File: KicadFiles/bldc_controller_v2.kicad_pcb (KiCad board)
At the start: 4 copper layers, 99.1 x 99.1 mm, 184 parts, among them J1 Conn_01x06_Male, J2 Screw_Terminal_01x04, Q1 2N7002E, Q10 IRLB8721PBF, Q11 IRLB8721PBF, Q2 DMN65D8L-7, Q3 DMN65D8L-7, Q4 MMBT3904, Q5 IRF4905, Q6 IRLB8721PBF, Q7 IRLB8721PBF, Q8 IRLB8721PBF, Q9 IRLB8721PBF, SW1 1301.9314, SW2 D6C50 F1 LFS, SW3 D6C40 F1 LFS, U1 ATmega328P-PU, U10 IRS2004, U2 SN74LVC1G11DBVR, U3 uA7810, U4 LM7805_TO220, U5 CD4044BE, U6 LM339, U7 MCP601-xP, U8 IRS2004, U9 IRS2004, Y1 9B-16.000MBBK-B

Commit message: Ready for Parts Placement
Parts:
- removed C37: 0.1uF, Capacitor_SMD:C_0805_2012Metric_Pad1.15x1.40mm_HandSolder
- removed R53: 0, Resistor_SMD:R_0805_2012Metric_Pad1.15x1.40mm_HandSolder
- removed REF** (x18): TestPoint_Plated_Hole_D2.0mm, TestPoint:TestPoint_Plated_Hole_D2.0mm
- removed RV1: 5K, Potentiometer_SMD:Trimmer_Pot_SM
- removed U10, U9: IRS2004, Package_DIP:DIP-8_W7.62mm
- added D7: LTST-C171GKT, LED_SMD:LED_0805_2012Metric_Pad1.15x1.40mm_HandSolder, F.Cu at (74.6, 36.0)
- added FB2: BL01RN1A1D2B, Ferrite_THT:Ferrite_Bead_TH, F.Cu at (50.0, 28.5)
- added J10: Conn_01x02_Female, Connector_PinHeader_2.54mm:PinHeader_1x02_P2.54mm_Vertical, F.Cu at (109.6, 18.1)
- added J11: Conn_01x02_Female, Connector_PinHeader_2.54mm:PinHeader_1x02_P2.54mm_Vertical, F.Cu at (100.4, 24.1)
- added J12: Conn_01x02_Female, Connector_PinHeader_2.54mm:PinHeader_1x02_P2.54mm_Vertical, F.Cu at (57.6, 67.4)
- added J13: Conn_01x02_Female, Connector_PinHeader_2.54mm:PinHeader_1x02_P2.54mm_Vertical, F.Cu at (94.4, 31.3)
- added J14: Conn_01x02_Female, Connector_PinHeader_2.54mm:PinHeader_1x02_P2.54mm_Vertical, F.Cu at (53.0, 67.4)
- added J15: Conn_01x04_Male, Connector_PinHeader_2.54mm:PinHeader_1x04_P2.54mm_Vertical, F.Cu at (41.4, 50.6)
- added J3: Conn_01x03_Male, Connector_PinHeader_2.54mm:PinHeader_1x03_P2.54mm_Vertical, F.Cu at (53.0, 57.7)
- added J4: Screw_Terminal, Connector:Terminal_Block_4Pin_TH, F.Cu at (60.5, 20.9)
- added J5: Conn_01x02_Female, Connector_PinHeader_2.54mm:PinHeader_1x02_P2.54mm_Vertical, F.Cu at (62.3, 57.7)
- added J9: Conn_01x02_Female, Connector_PinHeader_2.54mm:PinHeader_1x02_P2.54mm_Vertical, F.Cu at (95.8, 24.1)
- added JP2: SolderJumper_2_Open, Jumper:Solder_Jumper_2_Pin_5A, F.Cu at (118.0, 35.3)
- added SW4: 1301.9314, Button_Switch_SMD:Tactile_Switch_SM, F.Cu at (34.0, 47.0)
- added SW5: SW_Push_DPDT, Button_Switch_SMD:Slide_Switch_DPDT_SMD, F.Cu at (87.0, 33.2)
- added TP31: TestPoint, TestPoint:TestPoint_THTPad_1.0x1.0mm_Drill0.5mm, F.Cu at (105.3, 52.9)
- added TP32: TestPoint, TestPoint:TestPoint_THTPad_1.0x1.0mm_Drill0.5mm, F.Cu at (110.0, 49.8)
- added TP33: TestPoint, TestPoint:TestPoint_THTPad_1.0x1.0mm_Drill0.5mm, F.Cu at (114.5, 45.4)
- added TP34: TestPoint, TestPoint:TestPoint_THTPad_1.0x1.0mm_Drill0.5mm, F.Cu at (117.8, 42.3)
- added TP35: TestPoint, TestPoint:TestPoint_THTPad_1.0x1.0mm_Drill0.5mm, F.Cu at (85.1, 72.5)
- added TP36: TestPoint, TestPoint:TestPoint_THTPad_1.0x1.0mm_Drill0.5mm, F.Cu at (108.3, 52.9)
- added TP37: TestPoint, TestPoint:TestPoint_THTPad_1.0x1.0mm_Drill0.5mm, F.Cu at (118.6, 38.6)
- added TP38: TestPoint, TestPoint:TestPoint_THTPad_1.0x1.0mm_Drill0.5mm, F.Cu at (94.4, 67.1)
- C1, C2: value 10uF -> 47uF; footprint Capacitor_SMD:C_0805_2012Metric_Pad1.15x1.40mm_HandSolder -> Capacitor_THT:CP_Radial_D5.0mm_P2.00mm; moved to F.Cu
- C11: value 47uF -> 1uF; footprint Capacitor_THT:CP_Radial_D10.0mm_P5.00mm -> Capacitor_SMD:C_0805_2012Metric_Pad1.15x1.40mm_HandSolder
- C12, C23, C25, D11, D14, D15, D16, FB1, R21, R31, R33, R35, R37, R39, R40, R42: moved to F.Cu
- C13, C14, C22, C24, C3, C33: value 0.1uF -> 1uF; moved to F.Cu
- C15: value 22uF -> 22pF
- C16: value 1uF -> 22pF; moved to F.Cu
- C17, C21: value 1uF -> 0.1uF
- C18: value 22pF -> 0.1uF; moved to F.Cu
- C19: value 22pF -> 47uF; footprint Capacitor_SMD:C_0805_2012Metric_Pad1.15x1.40mm_HandSolder -> Capacitor_THT:CP_Radial_D5.0mm_P2.00mm; moved to F.Cu
- C20: value 0.1uF -> 1uF
- C26: value 0.1uF -> 15nF
- C27: value 10nF -> 0.1uF; moved to F.Cu
- C28, C29: value 22nF -> 0.1uF
- C30: value 22nF -> 1uF
- C31: value 1nF -> 1uF; moved to F.Cu
- C32: value 100pF -> 1uF; moved to F.Cu
- C34, C35: value 0.47uF -> 1uF
- C36: value 0.47uF -> 0.1uF
- C4: value 47uF -> 0.1uF; footprint Capacitor_THT:CP_Radial_D10.0mm_P5.00mm -> Capacitor_SMD:C_0805_2012Metric_Pad1.15x1.40mm_HandSolder
- C5: value 0.33uF -> 0.1uF; moved to F.Cu
- C6: value 0.22uF -> 0.1uF; moved to F.Cu
- C7: value 0.1uF -> 47uF; footprint Capacitor_SMD:C_0805_2012Metric_Pad1.15x1.40mm_HandSolder -> Capacitor_THT:CP_Radial_D5.0mm_P2.00mm
- C9: value 22uF -> 1uF
- D10: value BAT54HT1G -> LTST-C171TBKT; footprint Diode_SMD:D_SOD-323_HandSoldering -> LED_SMD:LED_0805_2012Metric_Pad1.15x1.40mm_HandSolder; moved to F.Cu
- D12: value SMF12A -> BAT54HT1G; footprint Diode_SMD:D_SOD-123F -> Diode_SMD:D_SOD-323_HandSoldering
- D13: value SMF5.0A -> BAT54HT1G; footprint Diode_SMD:D_SOD-123F -> Diode_SMD:D_SOD-323_HandSoldering
- D2: value LTST-C171KRKT -> SMF12A; footprint LED_SMD:LED_0805_2012Metric_Pad1.15x1.40mm_HandSolder -> Diode_SMD:D_SOD-123F
- D3, D6: value LTST-C171GKT -> LTST-C171KRKT
- D5: value LTST-C171KRKT -> SMF10A; footprint LED_SMD:LED_0805_2012Metric_Pad1.15x1.40mm_HandSolder -> Diode_SMD:D_SOD-123F
- D8: value SMF10A -> SMF5.0A
- D9: value LTST-C171TBKT -> LTST-C171GKT
- J2: value Screw_Terminal_01x04 -> Conn_01x03_Male; footprint Connector:Terminal_Block_4Pin_TH -> Connector_PinHeader_2.54mm:PinHeader_1x03_P2.54mm_Vertical
- Q1: value 2N7002E -> DMN65D8L-7
- Q4: value MMBT3904 -> DMN65D8L-7; moved to F.Cu
- R10, R13: value 300 -> 10K
- R11, R12: value 10K -> 100K; moved to F.Cu
- R14: value 10 -> 1K; moved to F.Cu
- R15: value 100K -> 50K; moved to F.Cu
- R16: value 1K -> 10K; moved to F.Cu
- R17: value 10K -> 1K; moved to F.Cu
- R19: value 3K -> 100K; moved to F.Cu
- R20: value 1K -> 100K
- R22: value 40K -> 100K
- R23: value 10K -> 0.47; footprint Resistor_SMD:R_0805_2012Metric_Pad1.15x1.40mm_HandSolder -> Resistor_THT:Power_Resistor_TH
- R24: value 1 -> 1K; footprint Resistor_THT:Power_Resistor_TH -> Resistor_SMD:R_0805_2012Metric_Pad1.15x1.40mm_HandSolder; moved to F.Cu
- R25: value 1 -> 0.47; moved to F.Cu
- R26, R27, R28: value 4.7 -> 10K; moved to F.Cu
- R29, R30: value 1 -> 10K; footprint Resistor_THT:Power_Resistor_TH -> Resistor_SMD:R_0805_2012Metric_Pad1.15x1.40mm_HandSolder; moved to F.Cu
- R32, R34, R36, R38: value 100K -> 10; moved to F.Cu
- R4: value 10K -> 300; moved to F.Cu
- R41: value 10 -> 100K; moved to F.Cu
- R43, R44, R45: value 10K -> 100K
- R46, R47, R48: value 1K -> 100K; moved to F.Cu
- R49, R50, R51, R9: value 1K -> 10K
- R52: value 0 -> 100; moved to F.Cu
- R6, R7: value 220 -> 300; moved to F.Cu
- R8: value 300 -> 10
- SW1: value 1301.9314 -> D6C50 F1 LFS; footprint Button_Switch_SMD:Tactile_Switch_SM -> Button_Switch_THT:Pushbutton_Switch_TH
- SW2: value D6C50 F1 LFS -> D6C40 F1 LFS
- SW3: value D6C40 F1 LFS -> 1301.9314; footprint Button_Switch_THT:Pushbutton_Switch_TH -> Button_Switch_SMD:Tactile_Switch_SM
- TP12, TP17, TP18, TP29: footprint TestPoint:TestPoint_Keystone_5000-5004_Miniature -> TestPoint:TestPoint_THTPad_1.0x1.0mm_Drill0.5mm
- U2: value SN74LVC1G11DBVR -> uA7810; footprint Package_TO_SOT_SMD:SOT-23-6_Handsoldering -> Package_TO_SOT_THT:TO-220-3_Vertical; moved to F.Cu
- U3: value uA7810 -> LM7805_TO220
- U4: value LM7805_TO220 -> MCP601-xP; footprint Package_TO_SOT_THT:TO-220-3_Vertical -> Package_DIP:DIP-8_W7.62mm
- U5: value CD4044BE -> LM339; footprint Package_DIP:DIP-16_W7.62mm -> Package_DIP:DIP-14_W7.62mm
- U6: value LM339 -> IRS2004; footprint Package_DIP:DIP-14_W7.62mm -> Package_DIP:DIP-8_W7.62mm
- U7: value MCP601-xP -> IRS2004
- moved U6 158.1 mm to (57.9, 28.0), turned to 0 degrees
- moved D16 142.8 mm to (43.4, 46.1), turned to 0 degrees
- moved D14 141.2 mm to (30.3, 49.9), turned to 0 degrees
- moved D15 141.1 mm to (36.1, 49.9), turned to 0 degrees
- moved C34 140.5 mm to (114.3, 17.3), turned to 0 degrees
- moved Q10 139.5 mm to (42.2, 70.4), turned to 0 degrees
- moved Q6 133.7 mm to (47.0, 53.4), turned to 0 degrees
- moved C35 131.9 mm to (99.1, 30.4), turned to 0 degrees
- moved R23 130.5 mm to (27.8, 56.0), turned to 0 degrees
- moved R49 129.9 mm to (76.7, 74.5), turned to 0 degrees
- moved U1 127.6 mm to (18.2, 17.9)
- moved C33 127.3 mm to (109.9, 24.5), turned to 0 degrees
- moved R25 124.4 mm to (27.8, 62.1), turned to 0 degrees
- moved TP16 123.4 mm to (122.0, 33.7)
- moved R21 123.1 mm to (38.7, 18.9), turned to 0 degrees
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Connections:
- C1 pad 1: /nRESET -> +BATT
- C1 pad 2: GNDD -> GNDPWR
- C10 pad 1: Vdrive -> +12V
- C10 pad 2: GNDPWR -> GNDD
- C11 pad 1: +12V -> +10V
- C11 pad 2: GNDPWR -> GNDD
- C12 pad 1: +5V -> +12V
- C12 pad 2: GNDD -> GNDPWR
- C13 pad 1: +10V -> /nSTART
- C14 pad 1: +5V -> /nESTOP
- C15 pad 1: +12V -> GNDD
- C15 pad 2: GNDPWR -> Net-(C15-Pad2)
- C17 pad 1: +12V -> +10V
- C17 pad 2: GNDPWR -> GNDD
- C18 pad 1: GNDD -> +5V
- C18 pad 2: Net-(C18-Pad2) -> GNDD
- C19 pad 1: Net-(C19-Pad1) -> /V_MOTOR
- C19 pad 2: GNDD -> GNDPWR
- C2 pad 1: /nESTOP -> VBUS
- C2 pad 2: GNDD -> GNDPWR
- C20 pad 1: +12V -> /V_MOTOR
- C21 pad 1: Vdrive -> /V_MOTOR
- C21 pad 2: Net-(C21-Pad2) -> GNDPWR
- C22 pad 1: +5V -> /AUX_IN
- C23 pad 1: GNDD -> +5V
- C23 pad 2: +10V -> GNDD
- C24 pad 1: GNDD -> /BTN_nRST
- C24 pad 2: +10V -> GNDD
- C25 pad 1: GNDD -> /V_MOTOR
- C25 pad 2: +10V -> /EFUSE_GATE
- C26 pad 1: +5V -> /I_FILT
- C27 pad 1: /I_RAW -> GNDD
- C27 pad 2: GNDD -> +10V
- C28 pad 1: Net-(C28-Pad1) -> GNDD
- C28 pad 2: PhaseA -> +10V
- C29 pad 1: Net-(C29-Pad1) -> GNDD
- C29 pad 2: PhaseB -> +10V
- C3 pad 1: Net-(C3-Pad1) -> VBUS
- C3 pad 2: GNDD -> GNDPWR
- C30 pad 2: PhaseC -> /PHASE_A
- C31 pad 1: /I_RAW -> Net-(C31-Pad1)
- C31 pad 2: GNDD -> /PHASE_B
- C32 pad 1: /I_RAW -> Net-(C32-Pad1)
- C32 pad 2: GNDD -> /PHASE_C
- C33 pad 1: +5V -> VBUS
- C33 pad 2: GNDD -> GNDPWR
- C34 pad 1: PhaseA -> VBUS
- C34 pad 2: GNDD -> GNDPWR
- C35 pad 1: PhaseB -> VBUS
- C35 pad 2: GNDD -> GNDPWR
- C36 pad 1: PhaseC -> +5V
- C4 pad 1: +BATT -> Net-(C4-Pad1)
- C4 pad 2: GNDPWR -> GNDD
- C5 pad 1: +12V -> VBUS
- C5 pad 2: GNDD -> GNDPWR
- C6 pad 1: +10V -> GNDD
- C6 pad 2: GNDD -> +5V
- C7 pad 1: GNDD -> +12V
- C7 pad 2: +5V -> GNDPWR
- C9 pad 1: Vdrive -> +12V
- D1 pad 2: +12V -> VBUS
- D10 pad 1: +5V -> Net-(D10-Pad1)
- D10 pad 2: /nRESET -> +5V
- D11 pad 2: /nESTOP -> /nSTART
- D12 pad 1: +12V -> +5V
- D12 pad 2: GNDD -> /nESTOP
- D13 pad 2: GNDD -> /BTN_nRST
- D14 pad 1: Net-(C28-Pad1) -> Net-(C30-Pad1)
- D15 pad 1: Net-(C29-Pad1) -> Net-(C31-Pad1)
- D16 pad 1: Net-(C30-Pad1) -> Net-(C32-Pad1)
- D2 pad 1: GNDD -> +12V
- D2 pad 2: Net-(D2-Pad2) -> GNDD
- D3 pad 2: VBUS -> +5V
- D4 pad 2: +10V -> +12V
- D5 pad 1: Net-(D5-Pad1) -> +10V
- D5 pad 2: +5V -> GNDD
- D8 pad 1: +10V -> +5V
- J1 pad 1: /nRESET -> /EXT_nRST
- J1 pad 2: /RXD -> +5V
- J1 pad 3: /TXD -> GNDD
- J1 pad 4: /ANALOG_IN -> GNDD
- J1 pad 5: +5V -> /TXD
- J1 pad 6: GNDD -> /RXD
- J2 pad 1: +BATT -> +5V
- J2 pad 2: Vdrive -> /I_THRESH
- J2 pad 3: GNDPWR -> GNDD
- JP1 pad 2: Vdrive -> /V_MOTOR
- Q1 pad 1: /nI_ERR -> /I_ERR
- Q1 pad 2: +5V -> GNDD
- Q10 pad 1: Net-(Q10-Pad1) -> /GATE_C_HI
- Q10 pad 3: PhaseC -> /PHASE_C
- Q11 pad 1: Net-(Q11-Pad1) -> /GATE_C_LO
- Q11 pad 2: PhaseC -> /PHASE_C
- Q5 pad 1: Net-(C21-Pad2) -> /EFUSE_GATE
- Q5 pad 3: Vdrive -> /V_MOTOR
- Q6 pad 1: Net-(Q6-Pad1) -> /GATE_A_HI
- Q6 pad 3: PhaseA -> /PHASE_A
- Q7 pad 1: Net-(Q7-Pad1) -> /GATE_A_LO
- Q7 pad 2: PhaseA -> /PHASE_A
- Q8 pad 1: Net-(Q8-Pad1) -> /GATE_B_HI
- Q8 pad 3: PhaseB -> /PHASE_B
- Q9 pad 1: Net-(Q9-Pad1) -> /GATE_B_LO
- Q9 pad 2: PhaseB -> /PHASE_B
- R10 pad 1: Net-(D6-Pad1) -> Net-(R10-Pad1)
- R11 pad 2: /nRESET -> /nSTART
- R13 pad 1: Net-(D9-Pad1) -> Net-(R13-Pad1)
- R13 pad 2: Net-(Q3-Pad3) -> GNDD
- R14 pad 1: Net-(R14-Pad1) -> Net-(Q4-Pad1)
- R14 pad 2: +10V -> /EFUSE_EN
- R15 pad 1: +5V -> /I_SENSE
- R15 pad 2: Net-(C16-Pad1) -> Net-(R15-Pad2)
- R16 pad 1: +5V -> Net-(R15-Pad2)
- R16 pad 2: /nI_ERR -> GNDD
- R17 pad 1: /EFUSE_EN -> +5V
- R17 pad 2: GNDD -> /nI_TRIG
- R18 pad 1: Vdrive -> Net-(Q4-Pad1)
- R18 pad 2: Net-(C21-Pad2) -> GNDD
- R19 pad 1: Net-(Q4-Pad1) -> /V_MOTOR
- R19 pad 2: /EFUSE_EN -> /EFUSE_GATE
- R2 pad 1: Net-(Q1-Pad3) -> Net-(D3-Pad1)
- R2 pad 2: Net-(D2-Pad2) -> Net-(Q1-Pad3)
- R20 pad 1: Net-(C21-Pad2) -> /AUX_IN
- R20 pad 2: Net-(Q4-Pad3) -> GNDD
- R22 pad 1: /I_SENSE -> +5V
- R22 pad 2: Net-(R22-Pad2) -> /BTN_nRST
- R23 pad 1: Net-(R22-Pad2) -> /I_RAW
- R23 pad 2: GNDD -> GNDPWR
- R24 pad 1: /I_RAW -> /EFUSE_GATE
- R24 pad 2: GNDPWR -> Net-(Q4-Pad3)
- R26 pad 1: Net-(D14-Pad2) -> +5V
- R26 pad 2: +10V -> Net-(R26-Pad2)
- R27 pad 1: Net-(D15-Pad2) -> /I_RAW
- R27 pad 2: +10V -> /I_FILT
- R28 pad 1: Net-(D16-Pad2) -> +5V
- R28 pad 2: +10V -> /BEMF_A
- R29 pad 1: /I_RAW -> +5V
- R29 pad 2: GNDPWR -> /BEMF_B
- R3 pad 1: Net-(D3-Pad1) -> Net-(D4-Pad1)
- R30 pad 1: /I_RAW -> +5V
- R30 pad 2: GNDPWR -> /BEMF_C
- R31 pad 1: Net-(Q6-Pad1) -> Net-(D14-Pad2)
- R31 pad 2: Net-(R31-Pad2) -> +10V
- R32 pad 1: Net-(Q6-Pad1) -> Net-(D15-Pad2)
- R32 pad 2: GNDD -> +10V
- R33 pad 1: Net-(Q7-Pad1) -> Net-(D16-Pad2)
- R33 pad 2: Net-(R33-Pad2) -> +10V
- R34 pad 1: Net-(Q7-Pad1) -> /GATE_A_LO
- R34 pad 2: GNDD -> Net-(R34-Pad2)
- R35 pad 1: Net-(Q8-Pad1) -> /GATE_B_LO
- R36 pad 1: Net-(Q8-Pad1) -> /GATE_C_LO
- R36 pad 2: GNDD -> Net-(R36-Pad2)
- R37 pad 1: Net-(Q9-Pad1) -> /GATE_A_HI
- R38 pad 1: Net-(Q9-Pad1) -> /GATE_B_HI
- R38 pad 2: GNDD -> Net-(R38-Pad2)
- R39 pad 1: Net-(Q10-Pad1) -> /GATE_C_HI
- R4 pad 1: /AUX_IN -> Net-(D6-Pad1)
- R4 pad 2: GNDD -> Net-(Q2-Pad3)
- R40 pad 1: Net-(Q10-Pad1) -> /GATE_A_HI
- R41 pad 1: Net-(Q11-Pad1) -> /GATE_A_LO
- R41 pad 2: Net-(R41-Pad2) -> GNDD
- R42 pad 1: Net-(Q11-Pad1) -> /GATE_B_HI
- R43 pad 1: /NEUTRAL -> /GATE_B_LO
- R43 pad 2: PhaseA -> GNDD
- R44 pad 1: /NEUTRAL -> /GATE_C_HI
- R44 pad 2: PhaseB -> GNDD
- R45 pad 1: /NEUTRAL -> /GATE_C_LO
- R45 pad 2: PhaseC -> GNDD
- R46 pad 1: +5V -> /PHASE_A
- R46 pad 2: /BEMF_A -> /A_FILT
- R47 pad 1: +5V -> /PHASE_B
- R47 pad 2: /BEMF_B -> /B_FILT
- R48 pad 1: +5V -> /PHASE_C
- R48 pad 2: /BEMF_C -> /C_FILT
- R49 pad 1: PhaseA -> /NEUTRAL
- R49 pad 2: Net-(R49-Pad2) -> /PHASE_A
- R5 pad 1: Net-(D4-Pad1) -> Net-(D7-Pad1)
- R50 pad 1: PhaseB -> /NEUTRAL
- R50 pad 2: Net-(R50-Pad2) -> /PHASE_B
- R51 pad 1: PhaseC -> /NEUTRAL
- R51 pad 2: Net-(R51-Pad2) -> /PHASE_C
- R52 pad 1: GNDPWR -> Net-(R52-Pad1)
- R52 pad 2: GNDD -> /nI_TRIG
- R6 pad 1: Net-(R6-Pad1) -> Net-(D9-Pad1)
- R7 pad 1: Net-(R7-Pad1) -> Net-(D10-Pad1)
- R7 pad 2: GNDD -> Net-(Q3-Pad3)
- R8 pad 1: Net-(D5-Pad1) -> Net-(R8-Pad1)
- R8 pad 2: Net-(Q2-Pad3) -> +10V
- R9 pad 1: +5V -> Net-(R9-Pad1)
- R9 pad 2: Net-(R9-Pad2) -> GNDD
- SW1 pad 1: /AUX_IN -> /nSTART
- SW1 pad 2: Net-(R9-Pad2) -> Net-(R9-Pad1)
- SW2 pad 1: /nRESET -> Net-(R10-Pad1)
- SW2 pad 2: Net-(R6-Pad1) -> /nESTOP
- SW3 pad 1: Net-(R7-Pad1) -> /BTN_nRST
- SW3 pad 2: /nESTOP -> Net-(R13-Pad1)
- TP1 pad 1: /I_RAW -> +12V
- TP10 pad 1: Net-(Q8-Pad1) -> /PHASE_A
- TP11 pad 1: Net-(Q10-Pad1) -> /EFUSE_GATE
- TP12 pad 1: GNDD -> /MCU_A_SIG
- TP13 pad 1: /BEMF_A -> /BEMF_B
- TP14 pad 1: /BEMF_B -> /I_FILT
- TP15 pad 1: /BEMF_C -> /GATE_A_LO
- TP16 pad 1: /NEUTRAL -> /PHASE_B
- TP17 pad 1: GNDD -> +5V
- TP18 pad 1: GNDPWR -> GNDD
- TP19 pad 1: /MCU_A_EN -> /EFUSE_EN
- TP2 pad 1: /nI_ERR -> GNDD
- TP20 pad 1: /MCU_C_SIG -> /MCU_B_EN
- TP21 pad 1: /MCU_B_SIG -> /BEMF_C
- TP22 pad 1: /MCU_A_SIG -> /I_SENSE
- TP23 pad 1: /MCU_C_EN -> /GATE_B_HI
- TP24 pad 1: /MCU_B_EN -> /PHASE_C
- TP25 pad 1: +12V -> /MCU_B_SIG
- TP26 pad 1: +10V -> /A_FILT
- TP27 pad 1: +5V -> /I_THRESH
- TP28 pad 1: Vdrive -> /GATE_B_LO
- TP29 pad 1: GNDD -> /MCU_C_EN
- TP3 pad 1: /EFUSE_EN -> +10V
- TP30 pad 1: /I_SENSE -> /B_FILT
- TP4 pad 1: Net-(RV1-Pad2) -> GNDD
- TP5 pad 1: Net-(C21-Pad2) -> /V_MOTOR
- TP6 pad 1: PhaseA -> /MCU_A_EN
- TP7 pad 1: PhaseB -> /BEMF_A
- TP8 pad 1: PhaseC -> /I_RAW
- TP9 pad 1: Net-(Q6-Pad1) -> /GATE_A_HI
- U1 pad 10: Net-(C19-Pad1) -> Net-(C16-Pad1)
- U1 pad 11: Net-(U1-Pad11) -> /I_ERR
- U1 pad 21: Net-(C3-Pad1) -> Net-(C4-Pad1)
- U1 pad 25: Net-(U1-Pad25) -> /I2C_SDA
- U1 pad 4: Net-(U1-Pad4) -> /nI_TRIG
- U1 pad 6: Net-(U1-Pad6) -> /I2C_SCL
- U1 pad 9: Net-(C18-Pad2) -> Net-(C15-Pad2)
- U2 pad 1: /nI_ERR -> +12V
- U2 pad 3: /nESTOP -> +10V
- U3 pad 1: +12V -> Net-(R8-Pad1)
- U3 pad 3: +10V -> +5V
- U4 pad 1: Net-(R14-Pad1) -> Net-(U4-Pad1)
- U4 pad 2: GNDD -> Net-(R15-Pad2)
- U4 pad 3: +5V -> /I_FILT
- U5 pad 1: Net-(U5-Pad1) -> /BEMF_A
- U5 pad 10: Net-(U5-Pad10) -> /NEUTRAL
- U5 pad 11: GNDD -> /C_FILT
- U5 pad 13: /EFUSE_EN -> /BEMF_C
- U5 pad 14: GNDD -> /BEMF_B
- U5 pad 2: Net-(U5-Pad2) -> Net-(R52-Pad1)
- U5 pad 3: /nRESET -> +5V
- U5 pad 4: Net-(U2-Pad4) -> /I_SENSE
- U5 pad 5: Net-(C16-Pad1) -> /I_THRESH
- U5 pad 6: GNDD -> /NEUTRAL
- U5 pad 7: GNDD -> /A_FILT
- U5 pad 8: GNDD -> /NEUTRAL
- U5 pad 9: Net-(U5-Pad9) -> /B_FILT
- U6 pad 1: /BEMF_A -> +10V
- U6 pad 2: /nI_ERR -> /MCU_A_SIG
- U6 pad 3: +5V -> /MCU_A_EN
- U6 pad 4: /I_SENSE -> GNDD
- U6 pad 5: Net-(RV1-Pad2) -> Net-(R34-Pad2)
- U6 pad 6: /NEUTRAL -> /PHASE_A
- U6 pad 7: Net-(R49-Pad2) -> Net-(R37-Pad2)
- U6 pad 8: /NEUTRAL -> Net-(C30-Pad1)
- U7 pad 1: Net-(U7-Pad1) -> +10V
- U7 pad 2: Net-(R22-Pad2) -> /MCU_B_SIG
- U7 pad 3: /I_RAW -> /MCU_B_EN
- U7 pad 5: Net-(U7-Pad5) -> Net-(R35-Pad2)
- U7 pad 6: /I_SENSE -> /PHASE_B
- U7 pad 7: +5V -> Net-(R38-Pad2)
- U7 pad 8: Net-(U7-Pad8) -> Net-(C31-Pad1)
- U8 pad 2: /MCU_A_SIG -> /MCU_C_SIG
- U8 pad 3: /MCU_A_EN -> /MCU_C_EN
- U8 pad 5: Net-(R33-Pad2) -> Net-(R36-Pad2)
- U8 pad 6: PhaseA -> /PHASE_C
- U8 pad 7: Net-(R31-Pad2) -> Net-(R39-Pad2)
- U8 pad 8: Net-(C28-Pad1) -> Net-(C32-Pad1)
- Y1 pad 1: Net-(C18-Pad2) -> Net-(C15-Pad2)
- Y1 pad 2: Net-(C19-Pad1) -> Net-(C16-Pad1)
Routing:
- net /nI_ERR: track 154.3 -> 0.00 mm
- net PhaseA: track 127.9 -> 0.00 mm, vias 18 -> 0
- net GNDD: track 126.1 -> 0.00 mm, vias 34 -> 0
- net +5V: track 118.2 -> 0.00 mm, vias 7 -> 0
- net /I_SENSE: track 113.9 -> 0.00 mm
- net VBUS: track 96.5 -> 0.00 mm, vias 1 -> 0
- net /BEMF_C: track 84.9 -> 0.00 mm
- net /BEMF_A: track 84.0 -> 0.00 mm
- net PhaseB: track 82.9 -> 0.00 mm, vias 20 -> 0
- net /nRESET: track 76.1 -> 0.00 mm
- net /BEMF_B: track 75.7 -> 0.00 mm
- net /I_RAW: track 74.1 -> 0.00 mm
- net Net-(R31-Pad2): track 67.2 -> 0.00 mm, vias 1 -> 0
- net Net-(R33-Pad2): track 62.3 -> 0.00 mm, vias 1 -> 0
- net PhaseC: track 60.1 -> 0.00 mm, vias 19 -> 0
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- removed copper zone on In1.Cu, net +10V
- removed copper zone on B.Cu, net +12V
- removed copper zone on F.Cu, net +12V
- removed copper zone on In1.Cu, net +5V
- removed copper zone on F.Cu, net +BATT
- removed copper zone on B.Cu, net /I_RAW
- removed copper zone on In2.Cu, net GNDD
- removed copper zone on In2.Cu, net GNDPWR
- removed copper zone on F.Cu, net Net-(F1-Pad1)
- removed copper zone on B.Cu, net PhaseA
- removed copper zone on F.Cu, net PhaseA
- removed copper zone on B.Cu, net PhaseB
- removed copper zone on F.Cu, net PhaseB
- removed copper zone on B.Cu, net PhaseC
- removed copper zone on F.Cu, net PhaseC
- removed copper zone on F.Cu, net VBUS
- removed copper zone on F.Cu, net Vdrive
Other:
- board size 99.1 x 99.1 mm -> 99 x 99 mm
- copper layers 4 -> 2
- board text removed: "10"
- board text removed: "10V"
- board text removed: "12"
- board text removed: "12V"
- board text removed: "5V"
- board text removed: "AIN"
- board text removed: "AUX"
- board text removed: "BEMFA"
- board text removed: "BEMFB"
- board text removed: "BEMFC"
- board text removed: "BLDC Motor Controller, EE 91, Fall 2019 Adi Telikicherla, Can (Sunny) Cui"
- board text removed: "DGND"
- board text removed: "EFS"
- board text removed: "EFS_EN"
- board text removed: "EFS_GATE"
- board text removed: "ESTOP"
- board text removed: "GAH"
- board text removed: "GBH"
- board text removed: "GCH"
- board text removed: "GND"
- board text removed: "I_RAW"
- board text removed: "I_SENSE"
- board text removed: "MCU_A_EN"
- board text removed: "MCU_A_SIG"
- board text removed: "MCU_B_EN"
- board text removed: "MCU_B_SIG"
- board text removed: "MCU_C_EN"
- board text removed: "MCU_C_SIG"
- board text removed: "NEUTRAL"
- board text removed: "OCR"
- board text removed: "OCR_THR"
- board text removed: "PGND"
- board text removed: "POWER"
- board text removed: "P_A"
- board text removed: "P_B"
- board text removed: "P_C"
- board text removed: "RESET"
- board text removed: "RX"
- board text removed: "STATUS"
- board text removed: "TX"
- board text removed: "VM"
- board text removed: "nI_ERR"
- board text removed: "nRST"

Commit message: Began Placement
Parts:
- C12, C20, C21, C3, C5, C9: moved to B.Cu
- moved Q5 108.7 mm to (148.5, 87.8), turned to 90 degrees
- moved F1 91.4 mm to (125.5, 70.0), turned to 180 degrees
- moved FB1 89.0 mm to (132.0, 67.5), turned to 180 degrees
- moved J4 80.7 mm to (118.0, 77.5), turned to 270 degrees
- moved C3 75.4 mm to (153.5, 64.0), turned to 90 degrees
- moved R19 74.6 mm to (145.0, 83.8), turned to 270 degrees
- moved C5 73.4 mm to (155.5, 64.0), turned to 90 degrees
- moved C9 72.7 mm to (139.5, 64.0), turned to 90 degrees
- moved C7 70.3 mm to (137.0, 65.0), turned to 90 degrees
- moved C2 69.3 mm to (151.0, 65.0), turned to 90 degrees
- moved C19 68.5 mm to (144.0, 65.0), turned to 90 degrees
- moved C20 68.3 mm to (146.5, 64.0), turned to 90 degrees
- moved R24 65.1 mm to (144.0, 87.8), turned to 180 degrees
- moved C1 61.7 mm to (124.0, 65.0), turned to 90 degrees
- moved C25 57.7 mm to (143.0, 83.8), turned to 270 degrees
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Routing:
- net (no net): vias 0 -> 2

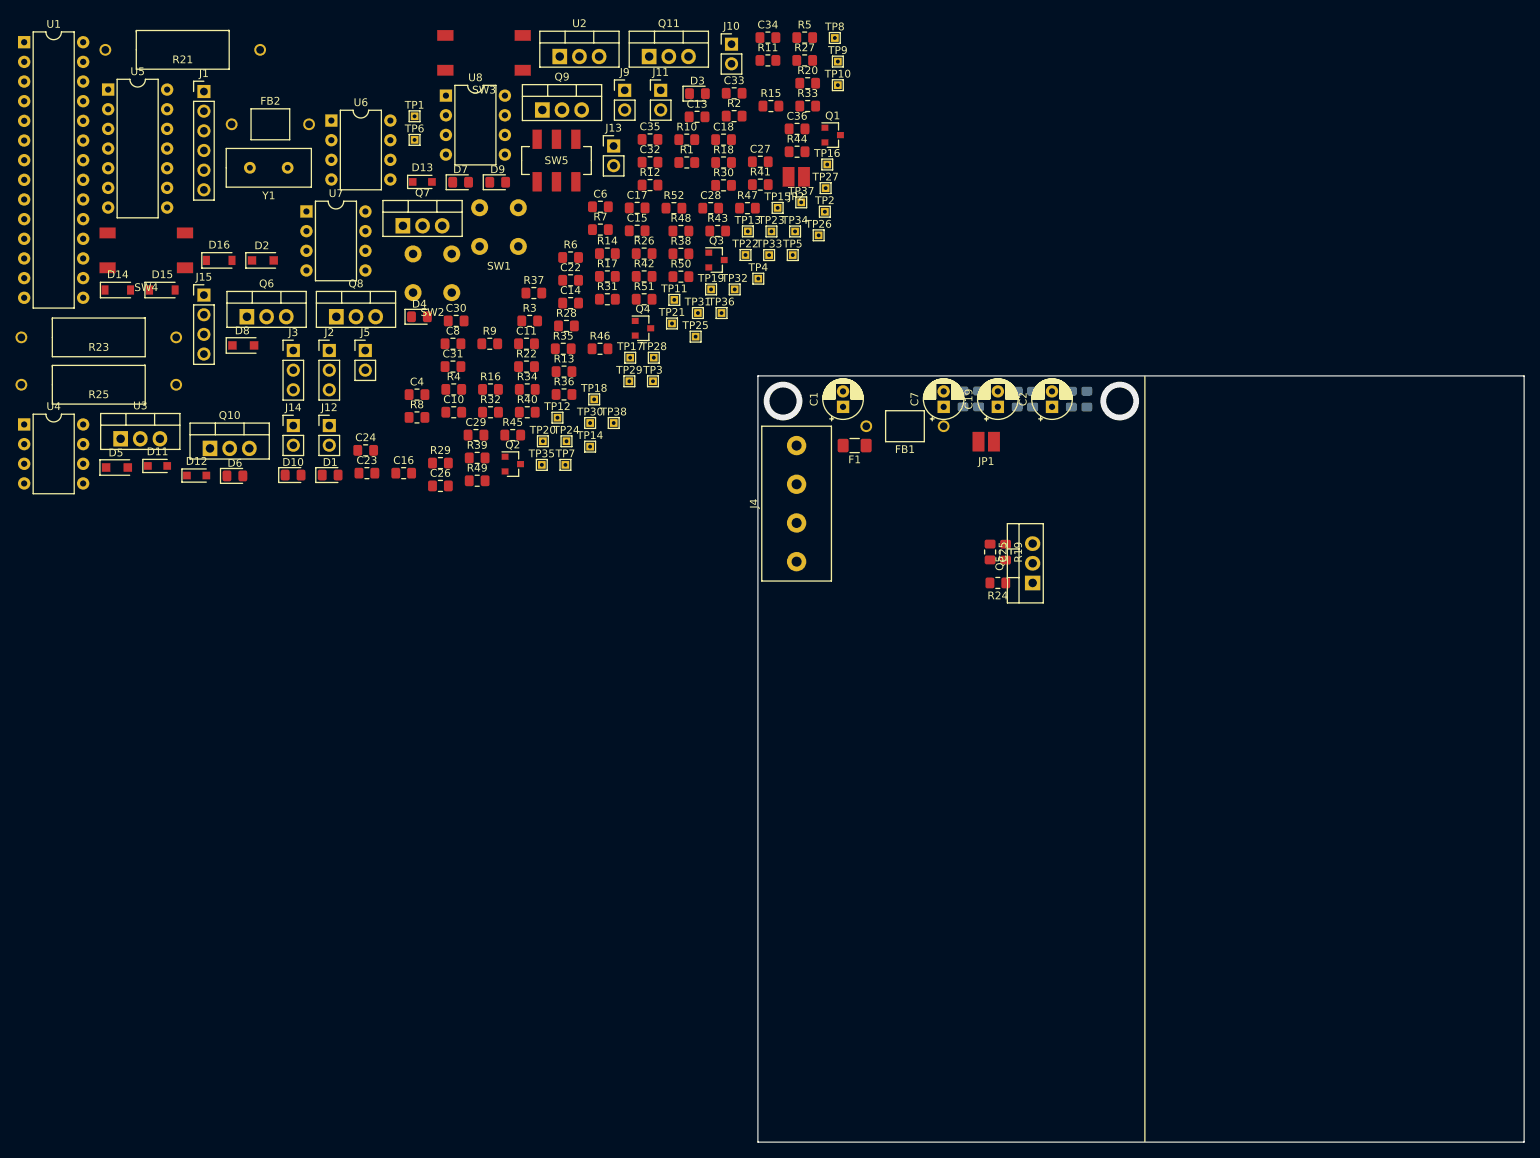
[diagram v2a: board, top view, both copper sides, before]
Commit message: Finished Placing Major Components
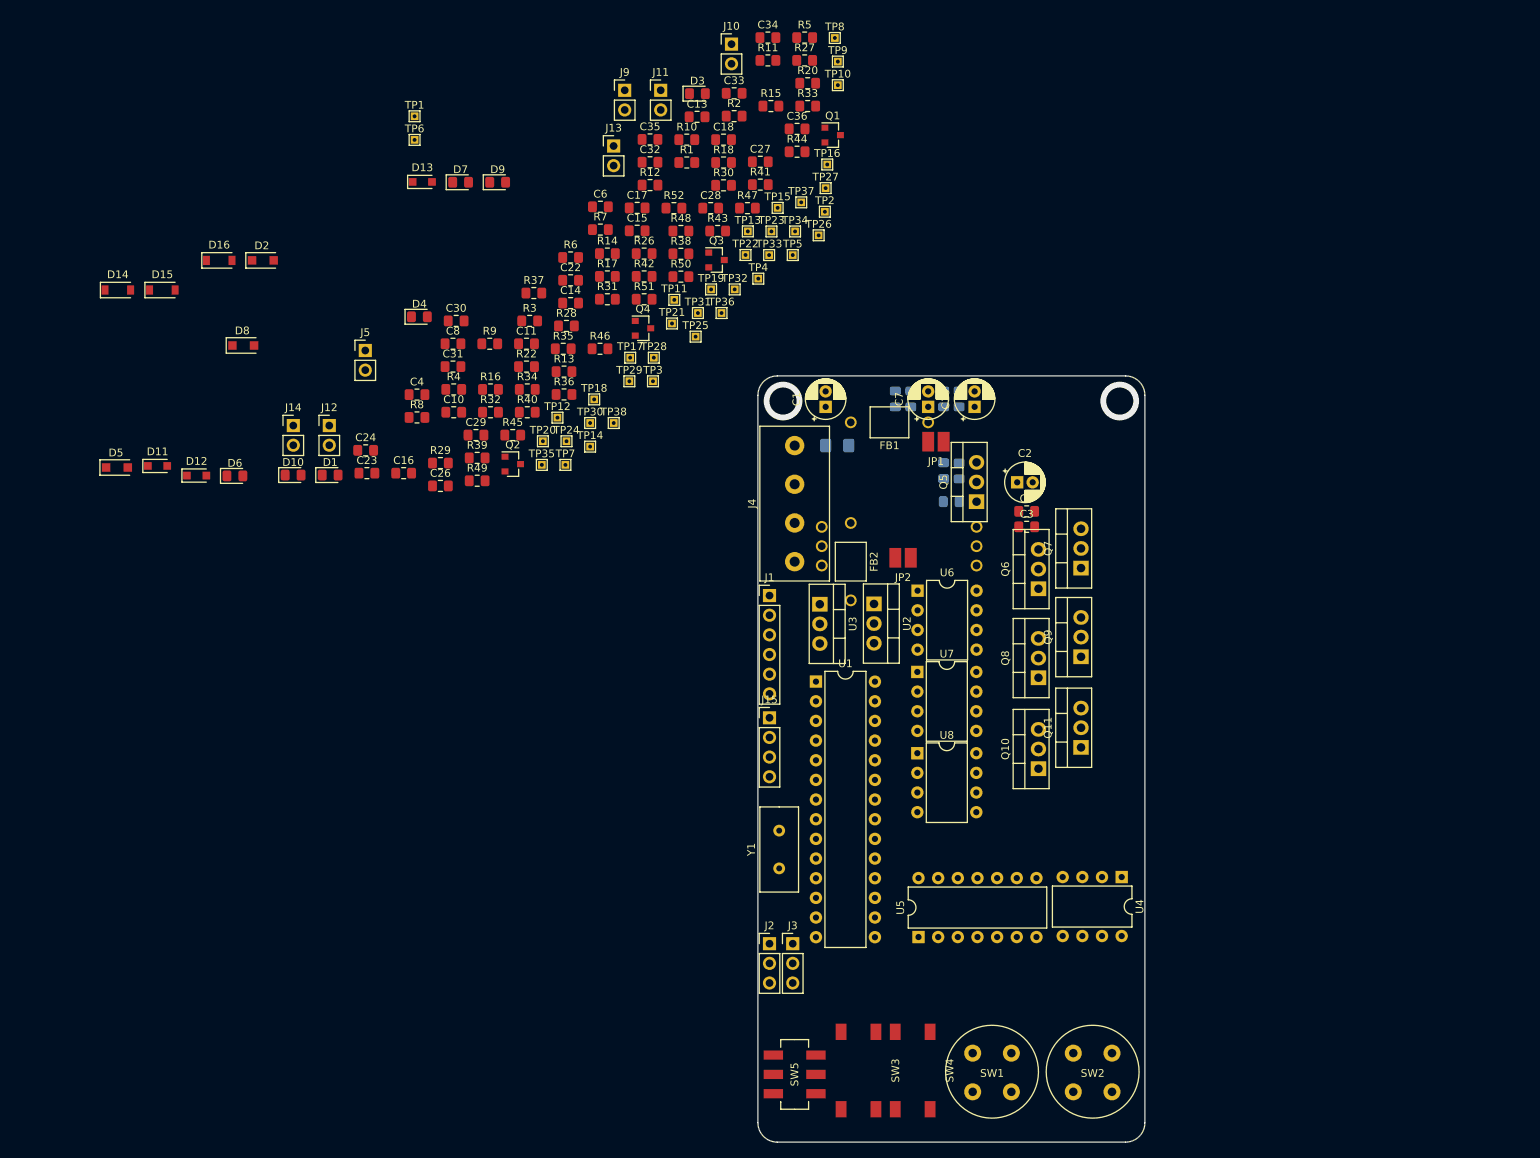
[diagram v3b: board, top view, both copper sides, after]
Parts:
- C25, F1, R19, R21, R23, R24, R25: moved to B.Cu
- C3, C5: moved to F.Cu
- moved U4 153.4 mm to (160.0, 125.8), turned to 270 degrees
- moved U5 151.5 mm to (133.8, 133.5), turned to 90 degrees
- moved SW4 145.0 mm to (135.2, 150.8), turned to 90 degrees
- moved SW3 138.8 mm to (128.2, 150.8), turned to 90 degrees
- moved SW2 133.9 mm to (156.2, 153.5)
- moved U1 131.5 mm to (120.5, 100.5)
- moved SW1 126.4 mm to (143.2, 153.5)
- moved SW5 122.0 mm to (117.8, 151.2), turned to 90 degrees
- moved Q10 114.8 mm to (149.2, 111.8), turned to 90 degrees
- moved R21 111.2 mm to (131.2, 80.5), turned to 180 degrees
- moved Y1 110.0 mm to (115.8, 122.2), turned to 270 degrees
- moved Q6 108.1 mm to (149.2, 88.5), turned to 90 degrees
- moved R23 107.5 mm to (131.2, 85.5), turned to 180 degrees
- moved R25 105.5 mm to (131.2, 83.0), turned to 180 degrees
- moved Q11 105.3 mm to (154.8, 109.0), turned to 90 degrees
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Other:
- board size 99 x 99 mm -> 50 x 99 mm

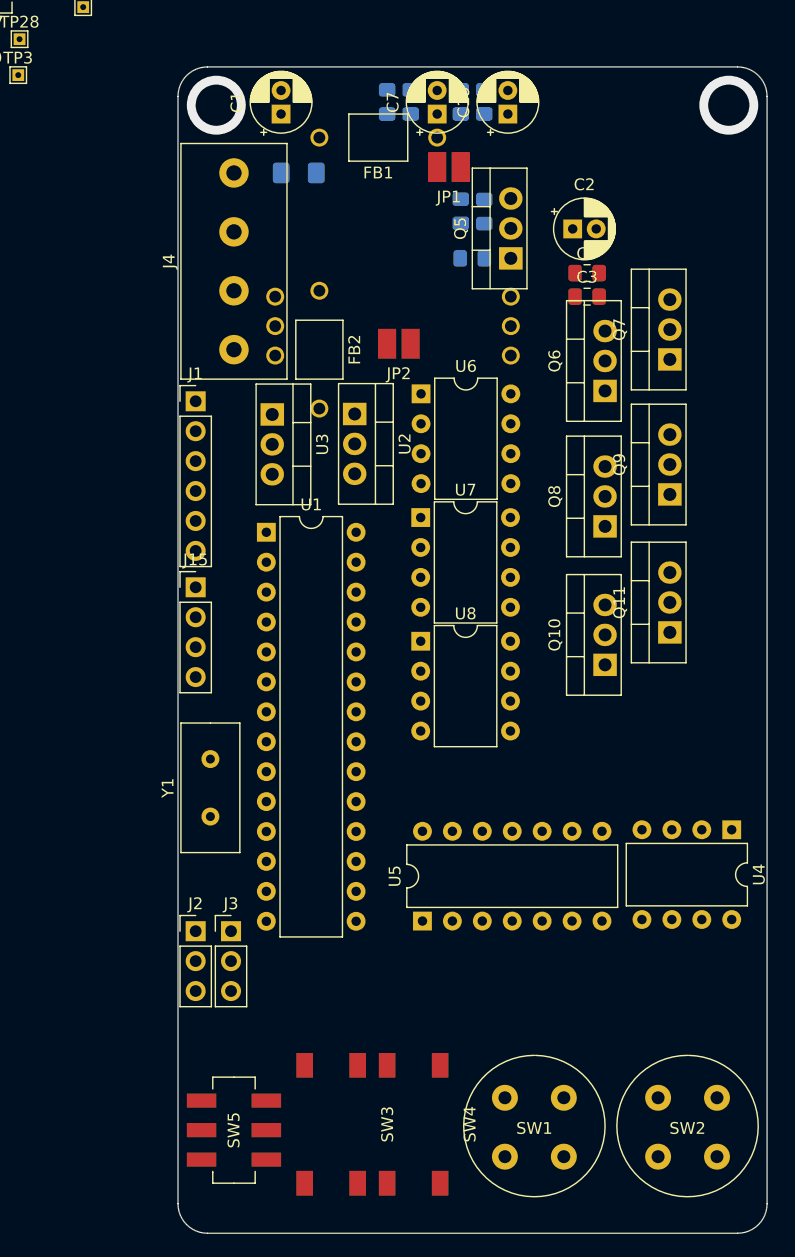
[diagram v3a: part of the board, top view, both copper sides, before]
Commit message: Added Optoisolator
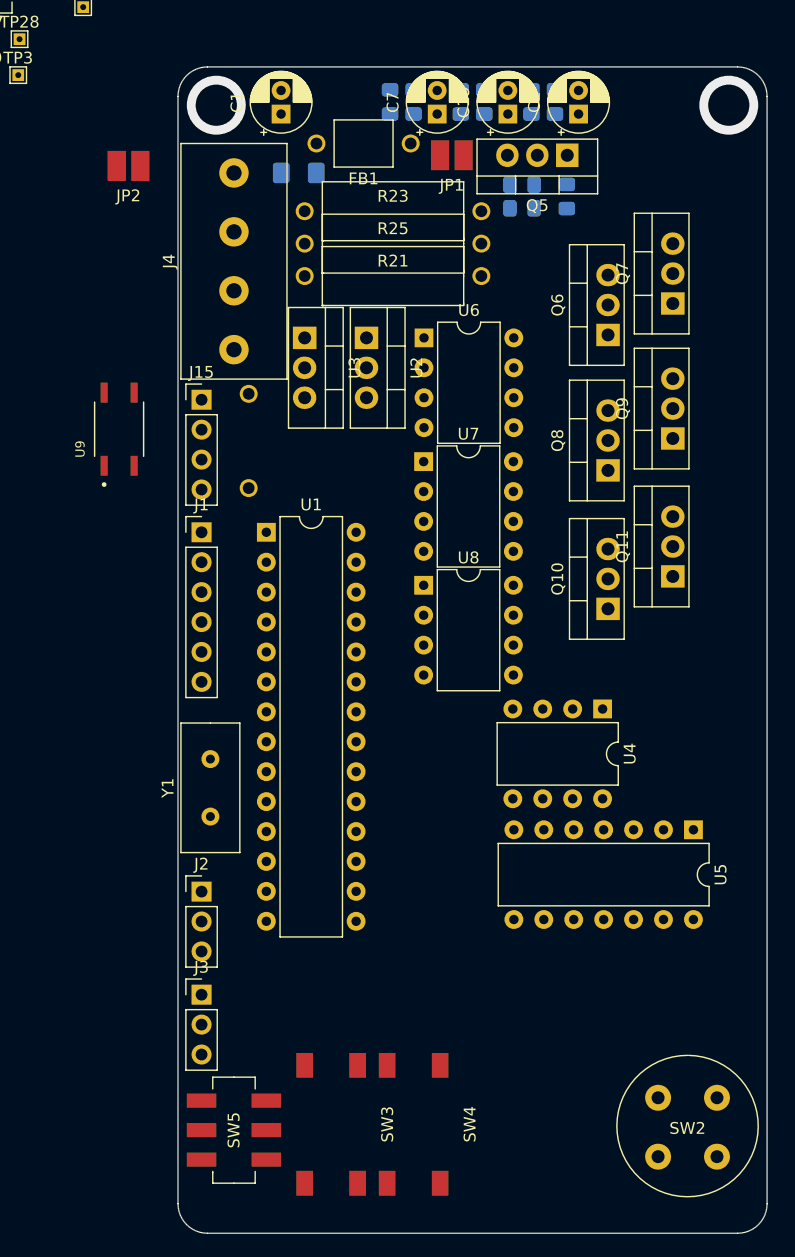
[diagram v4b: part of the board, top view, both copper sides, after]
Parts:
- removed SW1: D6C50 F1 LFS, Button_Switch_THT:Pushbutton_Switch_TH
- added U9: HCPL-181-00DE, HCPL-181:SOIC254P700X220-4N, F.Cu at (108.0, 91.8)
- C3, C5, FB2: moved to B.Cu
- R14: value 1K -> 150
- R21, R23, R25: moved to F.Cu
- moved JP2 27.5 mm to (108.8, 69.4)
- moved U5 24.3 mm to (156.8, 125.8), turned to 270 degrees
- moved C3 16.7 mm to (145.0, 64.0), turned to 90 degrees
- moved J15 15.9 mm to (115.0, 89.2)
- moved C5 15.3 mm to (143.0, 64.0), turned to 90 degrees
- moved U4 15.0 mm to (149.0, 115.5)
- moved R23 12.2 mm to (131.2, 73.2)
- moved J1 11.1 mm to (115.0, 100.5)
- moved Q5 9.98 mm to (146.0, 68.5), turned to 180 degrees
- moved FB2 9.80 mm to (119.0, 92.8)
- moved C2 9.76 mm to (147.0, 65.0), turned to 90 degrees
- moved R24 9.59 mm to (146.0, 72.0), turned to 270 degrees
- moved U3 7.06 mm to (123.8, 84.0)
- moved R25 7.00 mm to (131.2, 76.0)
- moved U2 6.54 mm to (129.0, 84.0)
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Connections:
- R14 pad 1: Net-(Q4-Pad1) -> Net-(R14-Pad1)
- R24 pad 2: Net-(Q4-Pad3) -> Net-(R24-Pad2)
- U1 pad 11: /I_ERR -> /nESTOP
- U1 pad 24: /ANALOG_IN -> /EFUSE_EN
- U1 pad 25: /I2C_SDA -> /ANALOG_IN
- U1 pad 27: /AUX_OUT -> /I2C_SDA
- U1 pad 28: /nMCU_ERR -> /I2C_SCL
- U1 pad 6: /I2C_SCL -> /AUX_OUT
